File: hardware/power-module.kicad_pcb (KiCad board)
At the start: 2 copper layers, 25 x 88 mm, 37 parts, among them CN1 WJ2EDGRC-5.08-2P, K1 SRA-9VDC-CL, K2 SRA-9VDC-CL, K5 SRA-9VDC-CL, K6 SRA-9VDC-CL, Q1 SS8050_C2150, Q2 SS8050_C2150, U1 MIC5205-3.3YM5-MS, U2 PM254-2-05-W-8.5, U3 CC6903SO-10A, U4 ESP32-C3-MINI-1, U5 XC6206P332MR_C5148692, U6 L7809CV_C347291

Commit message: Add PoE board
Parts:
- removed C3: 1uF, Capacitor_SMD:C_0603_1608Metric
- removed C4: 330nF, Capacitor_SMD:C_0603_1608Metric
- removed C5: 100nF, Capacitor_SMD:C_0603_1608Metric
- removed CN1: WJ2EDGRC-5.08-2P, LCSC:CONN-TH_2P-P5.08_WJ2EDGRC-5.08-2P
- removed H1: 2*5P header, LCSC:HDR-TH_10P-P2.54-H-M-R2-C5-S2.54-W12.9
- removed K5, K6: SRA-9VDC-CL, LCSC:RELAY-TH_SRA-9VDC-CL
- removed LED4: XL-1608UYC-06, LCSC:LED0603-RD-YELLOW
- removed R4, R5, R6: 10k, Resistor_SMD:R_0603_1608Metric
- removed R9: 120, Resistor_SMD:R_0603_1608Metric
- removed REF**: WEEE-Logo_4.2x6mm_SilkScreen, Symbol:WEEE-Logo_4.2x6mm_SilkScreen
- removed U2: PM254-2-05-W-8.5, LCSC:HDR-TH_10P-P2.54-H-F-R2-C5-W8.5
- added D4: ABS10_C65028, easyeda2kicad:ABS_L5.1-W4.4-P3.35-LS6.4-TL, F.Cu at (77.2, 37.3)
- added D5: ABS10_C65028, easyeda2kicad:ABS_L5.1-W4.4-P3.35-LS6.4-TL, F.Cu at (77.2, 44.3)
- added K3: SRA-12VDC-CL, easyeda2kicad:RELAY-TH_SRA-X-CX, F.Cu at (19.0, 30.0)
- added K4: SRA-12VDC-CL, easyeda2kicad:RELAY-TH_SRA-X-CX, F.Cu at (19.0, 43.0)
- added P1: WJ2EDGRC-5.08-4P, easyeda2kicad:CONN-TH_4P-P5.08_WJ2EDGRC-5.08-4P, F.Cu at (7.40, 36.0)
- added RJ2: S22-ZZ-0019, easyeda2kicad:RJ45-TH_RT7-ZZ-0117, F.Cu at (76.0, 21.0)
- added U7: DP9900LP-12V, easyeda2kicad:PWRM-TH_DP9900LP-5V, F.Cu at (60.0, 40.0)
- K1, K2: value SRA-9VDC-CL -> SRA-12VDC-CL; footprint LCSC:RELAY-TH_SRA-9VDC-CL -> easyeda2kicad:RELAY-TH_SRA-X-CX
- U4: value ESP32-C3-MINI-1 -> ESP32-U4WDH DUAL-CORE_C20622217; footprint PCM_Espressif:ESP32-C3-MINI-1 -> easyeda2kicad:QFN-48_L5.0-W5.0-P0.35-TL-EP3.7_ESP32-U4WDH
- U6: value L7809CV_C347291 -> LAN8720A-CP-TR; footprint LCSC:TO-220-3_L10.0-W4.5-P2.54-L -> easyeda2kicad:QFN-24_L4.0-W4.0-P0.50-BL-EP2.6
- moved LED5 148.5 mm to (181.9, 26.4), turned to 0 degrees
- moved LED2 147.8 mm to (181.9, 23.7), turned to 0 degrees
- moved LED1 145.4 mm to (181.9, 21.1), turned to 0 degrees
- moved U1 138.5 mm to (183.2, 15.7), turned to 0 degrees
- moved R10 134.3 mm to (171.2, 33.5), turned to 0 degrees
- moved R7 133.6 mm to (171.2, 31.0), turned to 0 degrees
- moved R3 131.1 mm to (171.2, 28.5), turned to 0 degrees
- moved U3 130.1 mm to (15.0, 17.0), turned to 0 degrees
- moved D1 129.9 mm to (180.5, 32.4), turned to 0 degrees
- moved D3 129.2 mm to (179.6, 40.7)
- moved Q1 128.6 mm to (175.3, 30.1), turned to 0 degrees
- moved D2 126.6 mm to (179.6, 38.1)
- moved C1 126.3 mm to (171.2, 21.0)
- moved C2 123.8 mm to (171.2, 23.5)
- moved Q2 123.1 mm to (175.3, 34.4), turned to 0 degrees
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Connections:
- C1 pad 1: /TRACK POWER IN -> +12V
- C2 pad 1: /CONTROLLER POWER IN -> +3.3V
- K1 pad 1: /TRACK POWER A -> /TRACK POWER ENABLED A
- K1 pad 2: Net-(D2-A) -> unconnected-(K1-Pad2)
- K1 pad 3: /TRACK POWER ENABLED A -> Net-(D2-A)
- K1 pad 4: unconnected-(K1-Pad4) -> /RELAY POWER
- K1 pad 5: /RELAY POWER -> /TRACK POWER A
- K2 pad 1: /TRACK POWER B -> /TRACK POWER ENABLED B
- K2 pad 2: /RELAY POWER -> unconnected-(K2-Pad2)
- K2 pad 3: /TRACK POWER ENABLED B -> /RELAY POWER
- K2 pad 4: unconnected-(K2-Pad4) -> Net-(D2-A)
- K2 pad 5: Net-(D2-A) -> /TRACK POWER B
- R3 pad 1: /CONTROLLER POWER IN -> +3.3V
- U1 pad 1: /TRACK POWER IN -> +12V
- U1 pad 3: /TRACK POWER IN -> +12V
- U1 pad 5: /CONTROLLER POWER IN -> +3.3V
- U4 pad 1: GND -> unconnected-(U4-VDDA-Pad1)
- U4 pad 11: GND -> unconnected-(U4-VDET_2-Pad11)
- U4 pad 14: GND -> unconnected-(U4-GPIO25-Pad14)
- U4 pad 16: Net-(U4-GPIO10) -> unconnected-(U4-GPIO27-Pad16)
- U4 pad 18: /CURRENT SENSING INPUT -> unconnected-(U4-MTDI-Pad18)
- U4 pad 2: GND -> unconnected-(U4-LNA_IN-Pad2)
- U4 pad 20: /TRACK POWER ENABLE -> unconnected-(U4-MTCK-Pad20)
- U4 pad 21: /TRACK DIRECTION -> unconnected-(U4-MTDO-Pad21)
- U4 pad 22: Net-(U4-GPIO8) -> unconnected-(U4-GPIO2-Pad22)
- U4 pad 23: /BOOT -> unconnected-(U4-GPIO0-Pad23)
- U4 pad 26: /USB - -> unconnected-(U4-VDD_SDIO-Pad26)
- U4 pad 27: /USB + -> unconnected-(U4-GPIO17-Pad27)
- U4 pad 3: /CONTROLLER POWER IN -> unconnected-(U4-VDD3P3-Pad3)
- U4 pad 36: GND -> unconnected-(U4-GPIO23-Pad36)
- U4 pad 37: GND -> unconnected-(U4-VDD3P3_CPU-Pad37)
- U4 pad 38: GND -> unconnected-(U4-GPIO19-Pad38)
- U4 pad 39: GND -> unconnected-(U4-GPIO22-Pad39)
- U4 pad 40: GND -> unconnected-(U4-U0RXD-Pad40)
- U4 pad 41: GND -> unconnected-(U4-U0TXD-Pad41)
- U4 pad 42: GND -> unconnected-(U4-GPIO21-Pad42)
- U4 pad 43: GND -> unconnected-(U4-VDDA-Pad43)
- U4 pad 44: GND -> unconnected-(U4-XTAL_N-Pad44)
- U4 pad 45: GND -> unconnected-(U4-XTAL_P-Pad45)
- U4 pad 46: GND -> unconnected-(U4-VDDA-Pad46)
- U4 pad 47: GND -> unconnected-(U4-CAP2-Pad47)
- U4 pad 48: GND -> unconnected-(U4-CAP1-Pad48)
- U4 pad 49: GND -> unconnected-(U4-GND-Pad49)
- U4 pad 5: Net-(U4-GPIO2/ADC1_CH2) -> unconnected-(U4-SENSOR_VP-Pad5)
- U4 pad 8: /RESET -> unconnected-(U4-SENSOR_VN-Pad8)
- U6 pad 1: /TRACK POWER IN -> unconnected-(U6-VDD2A-Pad1)
- U6 pad 2: GND -> unconnected-(U6-LED2/nINTSEL-Pad2)
- U6 pad 3: /RELAY POWER -> unconnected-(U6-LED1/REGOFF-Pad3)
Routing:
- net /CONTROLLER POWER IN: track 140.3 -> 0.00 mm, vias 5 -> 0
- net GND: track 101.8 -> 0.00 mm, vias 24 -> 0
- net /TRACK POWER B: track 90.2 -> 0.00 mm
- net /CURRENT SENSING INPUT: track 85.1 -> 0.00 mm, vias 4 -> 0
- net /TRACK POWER A: track 82.8 -> 0.00 mm
- net /RELAY POWER: track 78.4 -> 0.00 mm
- net Net-(D3-A): track 66.5 -> 0.00 mm, vias 4 -> 0
- net /TRACK POWER IN: track 51.2 -> 0.00 mm, vias 2 -> 0
- net /TRACK DIRECTION: track 44.7 -> 0.00 mm, vias 2 -> 0
- net /TRACK POWER ENABLE: track 44.7 -> 0.00 mm, vias 3 -> 0
- net /TRACK POWER ENABLED B: track 43.1 -> 0.00 mm
- net Net-(U4-GPIO10): track 30.7 -> 0.00 mm, vias 2 -> 0
- net Net-(D2-A): track 30.4 -> 0.00 mm, vias 2 -> 0
- net /RESET: track 30.2 -> 0.00 mm, vias 2 -> 0
- net /TRACK POWER ENABLED A: track 28.5 -> 0.00 mm
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- removed copper zone on B.Cu, net GND
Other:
- board size 25 x 88 mm -> 85 x 50 mm
- board text removed: "12V - 24V DC 8A"
- board text removed: "8A = 70°C"
- board text removed: "ACT"
- board text removed: "DIR"
- board text removed: "ENA"
- board text removed: "PRG"
- board text removed: "PWR"
- board text removed: "networked power module"
- board text removed: "v2b"

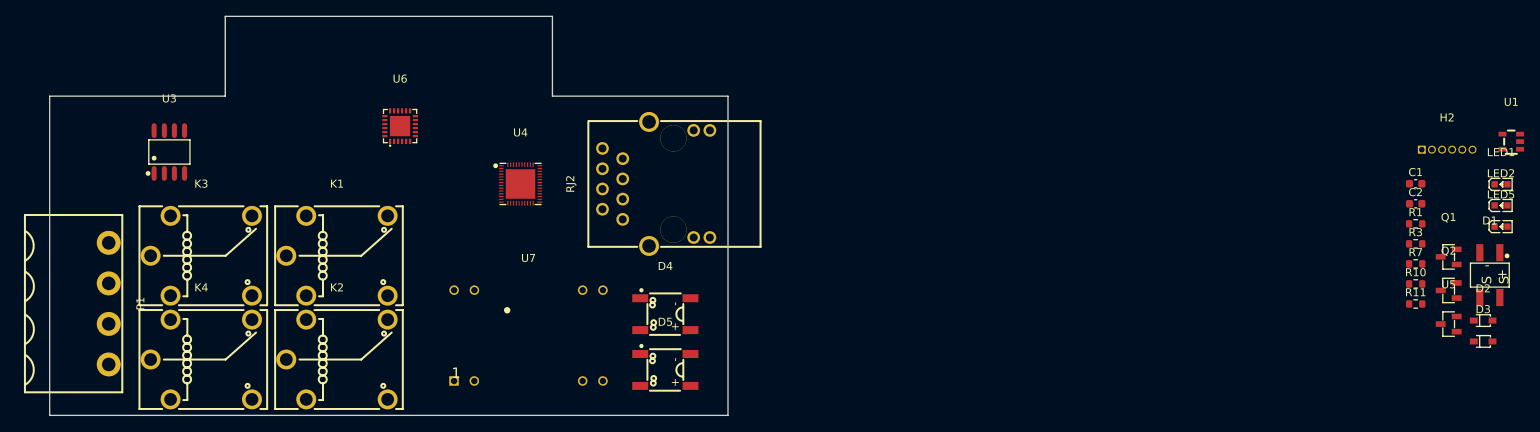
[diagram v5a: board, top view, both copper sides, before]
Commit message: Add routes and part placement
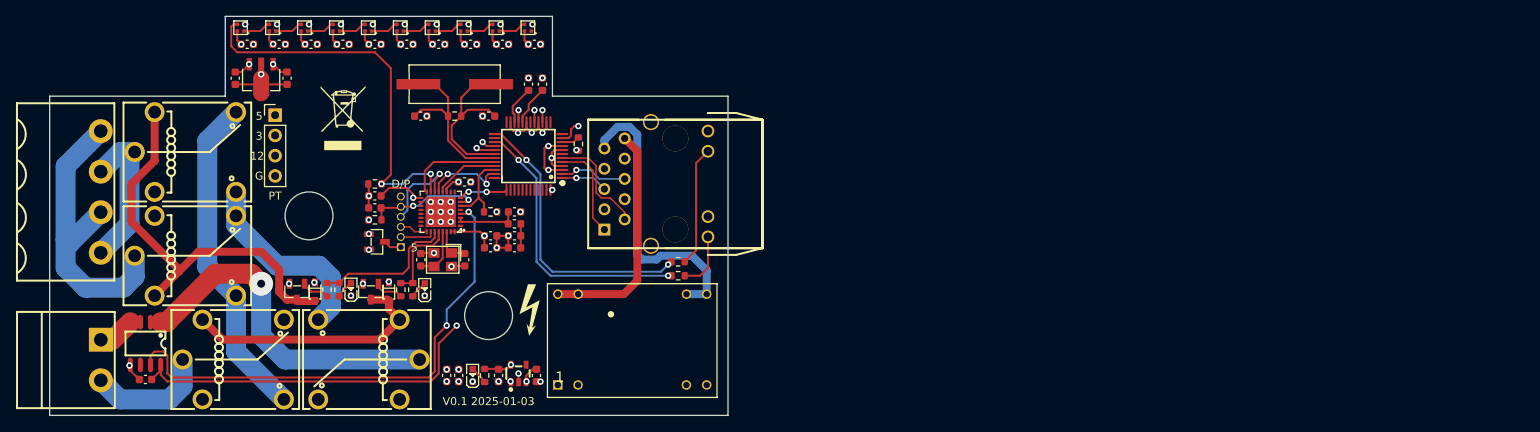
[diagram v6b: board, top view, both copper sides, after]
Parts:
- removed D3: BAS321,115, LCSC:SOD-323_L1.8-W1.3-LS2.5-RD
- removed D4, D5: ABS10_C65028, easyeda2kicad:ABS_L5.1-W4.4-P3.35-LS6.4-TL
- removed H2: DZ127R-11-06-25, LCSC:HDR-TH_6P-P1.27-V-M-A
- removed LED5: XL-1608UYC-06, LCSC:LED0603-RD-YELLOW
- removed RJ2: S22-ZZ-0019, easyeda2kicad:RJ45-TH_RT7-ZZ-0117
- added C10: 0.1uF, Capacitor_SMD:C_0603_1608Metric, F.Cu at (24.8, 3.50)
- added C11: 0.1uF, Capacitor_SMD:C_0603_1608Metric, F.Cu at (28.8, 3.50)
- added C12: 0.1uF, Capacitor_SMD:C_0603_1608Metric, F.Cu at (32.8, 3.50)
- added C13: 0.1uF, Capacitor_SMD:C_0603_1608Metric, F.Cu at (36.8, 3.50)
- added C14: 0.1uF, Capacitor_SMD:C_0603_1608Metric, F.Cu at (40.8, 3.50)
- added C15: 0.1uF, Capacitor_SMD:C_0603_1608Metric, F.Cu at (44.8, 3.50)
- added C16: 1uF, Capacitor_SMD:C_0603_1608Metric, F.Cu at (52.0, 30.5)
- added C17: 1uF, Capacitor_SMD:C_0603_1608Metric, F.Cu at (46.5, 30.5)
- added C18: 0.33uF, Capacitor_SMD:C_0603_1608Metric, F.Cu at (23.2, 7.75)
- added C19: 0.1uF, Capacitor_SMD:C_0603_1608Metric, F.Cu at (29.8, 7.75)
- added C20: 0.1nF, Capacitor_SMD:C_0603_1608Metric, F.Cu at (12.0, 45.5)
- added C21: 1uF, Capacitor_SMD:C_0603_1608Metric, F.Cu at (55.2, 29.0)
- added C22: 10nF, Capacitor_SMD:C_0603_1608Metric, F.Cu at (55.2, 27.5)
- added C23: 0.1uF, Capacitor_SMD:C_0603_1608Metric, F.Cu at (52.0, 20.8)
- added C24: 0.1uF, Capacitor_SMD:C_0603_1608Metric, F.Cu at (40.8, 22.5)
- added C25: 1uF, Capacitor_SMD:C_0603_1608Metric, F.Cu at (58.2, 24.5)
- added C26: 0.1uF, Capacitor_SMD:C_0603_1608Metric, F.Cu at (58.2, 27.5)
- added C27: 10uF, Capacitor_SMD:C_0603_1608Metric, F.Cu at (58.2, 29.0)
- added C28: 0.1uF, Capacitor_SMD:C_0603_1608Metric, F.Cu at (48.8, 3.50)
- added C29: 0.1uF, Capacitor_SMD:C_0603_1608Metric, F.Cu at (52.8, 3.50)
- added C3: 100uF 25V, Capacitor_SMD:C_0603_1608Metric, F.Cu at (49.8, 45.0)
- added C30: 0.1uF, Capacitor_SMD:C_0603_1608Metric, F.Cu at (56.8, 3.50)
- added C31: 0.1uF, Capacitor_SMD:C_0603_1608Metric, F.Cu at (60.8, 3.50)
- added C4: 10uF 25V, Capacitor_SMD:C_0603_1608Metric, F.Cu at (51.2, 45.0)
- added C5: 4.7uF, Capacitor_SMD:C_0603_1608Metric, F.Cu at (61.8, 8.50)
- added C6: 4.7uF, Capacitor_SMD:C_0603_1608Metric, F.Cu at (60.0, 8.50)
- added C7: 4.7uF, Capacitor_SMD:C_0603_1608Metric, F.Cu at (55.0, 12.5)
- added C8: 4.7uF, Capacitor_SMD:C_0603_1608Metric, F.Cu at (46.5, 12.5)
- added C9: 1uF, Capacitor_SMD:C_0603_1608Metric, F.Cu at (40.8, 24.0)
- added CN1: WJ2EDGRC-5.08-2P, easyeda2kicad:CONN-TH_2P-P5.08_WJ2EDGRC-5.08-2P, F.Cu at (6.41, 43.1)
- added H1: DZ127R-11-06-25, easyeda2kicad:HDR-TH_6P-P1.27-V-M-A, F.Cu at (44.0, 25.8)
- added J1: Conn_01x04_Pin, Connector_PinHeader_2.54mm:PinHeader_1x04_P2.54mm_Vertical, F.Cu at (28.2, 12.4)
- added L1: 2.0nH, Inductor_SMD:L_0603_1608Metric, F.Cu at (58.2, 26.0)
- added LED3: XL-1608UYC-06, easyeda2kicad:LED0603-RD-YELLOW, F.Cu at (37.8, 34.2)
- added R12: 10K, Resistor_SMD:R_0603_1608Metric, F.Cu at (40.8, 21.0)
- added R2: 56, Resistor_SMD:R_0603_1608Metric, F.Cu at (78.8, 32.5)
- added R4: 56, Resistor_SMD:R_0603_1608Metric, F.Cu at (78.8, 30.8)
- added R5: 12.4K 1%, Resistor_SMD:R_0603_1608Metric, F.Cu at (66.2, 16.0)
- added R6: 1M, Resistor_SMD:R_0603_1608Metric, F.Cu at (50.8, 12.5)
- added R8: 10K, Resistor_SMD:R_0603_1608Metric, F.Cu at (55.2, 24.5)
- added R9: 10K, Resistor_SMD:R_0603_1608Metric, F.Cu at (40.8, 25.5)
- added REF**: WEEE-Logo_5.6x8mm_SilkScreen, Symbol:WEEE-Logo_5.6x8mm_SilkScreen, F.Cu at (36.8, 12.8)
- added RJ1: HY931147C, easyeda2kicad:RJ45-TH_HY931147C, F.Cu at (76.0, 21.0)
- added U10: XL-1010RGBC-WS2812B, easyeda2kicad:LED-SMD_4P-L1.0-W1.0-TL_XL-1010RGBC-WS2812B, F.Cu at (35.9, 1.42)
- added U11: XL-1010RGBC-WS2812B, easyeda2kicad:LED-SMD_4P-L1.0-W1.0-TL_XL-1010RGBC-WS2812B, F.Cu at (39.9, 1.42)
- added U12: XL-1010RGBC-WS2812B, easyeda2kicad:LED-SMD_4P-L1.0-W1.0-TL_XL-1010RGBC-WS2812B, F.Cu at (43.9, 1.42)
- added U13: L327S400H11L, easyeda2kicad:CRYSTAL-SMD_4P-L3.2-W2.5-BL, F.Cu at (49.2, 30.5)
- added U14: UMW78L05, easyeda2kicad:SOT-89-3_L4.5-W2.5-P1.50-LS4.2-BR, F.Cu at (26.5, 7.36)
- added U15: XL-1010RGBC-WS2812B, easyeda2kicad:LED-SMD_4P-L1.0-W1.0-TL_XL-1010RGBC-WS2812B, F.Cu at (47.9, 1.42)
- added U16: XL-1010RGBC-WS2812B, easyeda2kicad:LED-SMD_4P-L1.0-W1.0-TL_XL-1010RGBC-WS2812B, F.Cu at (51.9, 1.42)
- added U17: XL-1010RGBC-WS2812B, easyeda2kicad:LED-SMD_4P-L1.0-W1.0-TL_XL-1010RGBC-WS2812B, F.Cu at (55.9, 1.42)
- added U18: XL-1010RGBC-WS2812B, easyeda2kicad:LED-SMD_4P-L1.0-W1.0-TL_XL-1010RGBC-WS2812B, F.Cu at (59.9, 1.42)
- added U2: CC6903SO-10A, easyeda2kicad:SOP-8_L4.9-W3.9-P1.27-LS6.0-BL, F.Cu at (12.0, 41.0)
- added U8: XL-1010RGBC-WS2812B, easyeda2kicad:LED-SMD_4P-L1.0-W1.0-TL_XL-1010RGBC-WS2812B, F.Cu at (27.9, 1.42)
- added U9: XL-1010RGBC-WS2812B, easyeda2kicad:LED-SMD_4P-L1.0-W1.0-TL_XL-1010RGBC-WS2812B, F.Cu at (31.9, 1.42)
- added X1: X49SM25MSD2SC, easyeda2kicad:HC-49S_L11.4-W4.8, F.Cu at (50.8, 8.50)
- D1: value MB10FH5G0NP -> BAS321,115; footprint LCSC:MBF_L4.8-W3.9-P2.50-LS6.7-TR -> easyeda2kicad:SOD-323_L1.8-W1.3-LS2.5-RD
- D2: footprint LCSC:SOD-323_L1.8-W1.3-LS2.5-RD -> easyeda2kicad:SOD-323_L1.8-W1.3-LS2.5-RD
- LED1, LED2: footprint LCSC:LED0603-RD-YELLOW -> easyeda2kicad:LED0603-RD-YELLOW
- Q1, Q2, U5: footprint LCSC:SOT-23-3_L2.9-W1.3-P1.90-LS2.4-BR -> easyeda2kicad:SOT-23-3_L2.9-W1.3-P1.90-LS2.4-BR
- U1: footprint LCSC:SOT-23-5_L2.9-W1.6-P0.95-LS2.8-BR -> easyeda2kicad:SOT-23-5_L2.9-W1.6-P0.95-LS2.8-BR
- U3: value CC6903SO-10A -> W5500; footprint LCSC:SOP-8_L4.9-W3.9-P1.27-LS6.0-BL -> easyeda2kicad:LQFP-48_L7.0-W7.0-P0.50-LS9.0-BL
- U4: value ESP32-U4WDH DUAL-CORE_C20622217 -> ESP32-C3FH4; footprint easyeda2kicad:QFN-48_L5.0-W5.0-P0.35-TL-EP3.7_ESP32-U4WDH -> easyeda2kicad:QFN-32_L5.0-W5.0-P0.50-TL-EP3.7
- U6: value LAN8720A-CP-TR -> XL-1010RGBC-WS2812B; footprint easyeda2kicad:QFN-24_L4.0-W4.0-P0.50-BL-EP2.6 -> easyeda2kicad:LED-SMD_4P-L1.0-W1.0-TL_XL-1010RGBC-WS2812B
- moved D2 146.4 mm to (33.2, 34.5), turned to -90 degrees
- moved Q1 144.4 mm to (31.0, 34.5), turned to 90 degrees
- moved D1 138.0 mm to (42.5, 34.5), turned to -90 degrees
- moved R11 136.4 mm to (34.8, 34.2), turned to 90 degrees
- moved LED2 135.3 mm to (47.0, 34.2), turned to 90 degrees
- moved Q2 135.1 mm to (40.2, 34.5), turned to 90 degrees
- moved R10 134.9 mm to (36.2, 34.2), turned to 90 degrees
- moved U5 134.7 mm to (41.0, 28.2), turned to 180 degrees
- moved LED1 131.1 mm to (53.0, 45.0), turned to 90 degrees
- moved U1 127.7 mm to (58.8, 44.8), turned to -90 degrees
- moved R1 127.4 mm to (44.0, 34.2), turned to 90 degrees
- moved R7 125.7 mm to (45.5, 34.2), turned to 90 degrees
- moved R3 117.8 mm to (54.5, 45.0), turned to -90 degrees
- moved C2 116.9 mm to (56.2, 45.0), turned to -90 degrees
- moved C1 112.8 mm to (61.0, 45.0), turned to -90 degrees
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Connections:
- D1 pad 1: /TRACK POWER IN -> +12V
- D1 pad 2: /TRACK POWER A -> Net-(D1-A)
- D2 pad 1: /RELAY POWER -> +12V
- K1 pad 3: Net-(D2-A) -> Net-(D1-A)
- K1 pad 4: /RELAY POWER -> +12V
- K2 pad 3: /RELAY POWER -> +12V
- K2 pad 4: Net-(D2-A) -> Net-(D1-A)
- K3 pad 3: Net-(D3-A) -> Net-(D2-A)
- K3 pad 4: /RELAY POWER -> +12V
- K4 pad 3: /RELAY POWER -> +12V
- K4 pad 4: Net-(D3-A) -> Net-(D2-A)
- P1 pad 2: Net-(P1-Pad2) -> /TRACK OUT A
- P1 pad 4: Net-(P1-Pad2) -> /TRACK OUT A
- Q1 pad 3: Net-(D3-A) -> Net-(D2-A)
- Q2 pad 3: Net-(D2-A) -> Net-(D1-A)
- U3 pad 1: /TRACK OUT A -> /ETHERNET TX -
- U3 pad 2: /TRACK OUT A -> /ETHERNET TX +
- U3 pad 3: Net-(P1-Pad2) -> GND
- U3 pad 4: Net-(P1-Pad2) -> +3.3V
- U3 pad 5: GND -> /ETHERNET RX -
- U3 pad 6: unconnected-(U3-NC-Pad6) -> /ETHERNET RX +
- U3 pad 7: /CURRENT SENSING INPUT -> unconnected-(U3-DNC-Pad7)
- U3 pad 8: /CONTROLLER POWER IN -> +3.3V
- U4 pad 11: unconnected-(U4-VDET_2-Pad11) -> +3.3V
- U4 pad 12: unconnected-(U4-32K_XP-Pad12) -> /WIZ SPI SCLK
- U4 pad 13: unconnected-(U4-32K_XN-Pad13) -> /WIZ SPI MOSI
- U4 pad 14: unconnected-(U4-GPIO25-Pad14) -> /BOOT
- U4 pad 15: unconnected-(U4-GPIO26-Pad15) -> /LED DATA IN
- U4 pad 16: unconnected-(U4-GPIO27-Pad16) -> /WIZ SPI CS
- U4 pad 17: unconnected-(U4-MTMS-Pad17) -> +3.3V
- U4 pad 2: unconnected-(U4-LNA_IN-Pad2) -> Net-(C25-Pad2)
- U4 pad 25: unconnected-(U4-GPIO16-Pad25) -> /USB -
- U4 pad 26: unconnected-(U4-VDD_SDIO-Pad26) -> /USB +
- U4 pad 27: unconnected-(U4-GPIO17-Pad27) -> /TRACK DIRECTION
- U4 pad 28: unconnected-(U4-SD_DATA_2-Pad28) -> /TRACK POWER ENABLE
- U4 pad 29: unconnected-(U4-SD_DATA_3-Pad29) -> Net-(U4-XTAL_N)
- U4 pad 3: unconnected-(U4-VDD3P3-Pad3) -> Net-(C25-Pad2)
- U4 pad 30: unconnected-(U4-SD_CMD-Pad30) -> Net-(U4-XTAL_P)
- U4 pad 31: unconnected-(U4-SD_CLK-Pad31) -> +3.3V
- U4 pad 32: unconnected-(U4-SD_DATA_0-Pad32) -> +3.3V
- U4 pad 33: unconnected-(U4-SD_DATA_1-Pad33) -> GND
- U4 pad 4: unconnected-(U4-VDD3P3-Pad4) -> /CURRENT SENSING INPUT
- U4 pad 6: unconnected-(U4-SENSOR_CAPP-Pad6) -> /WIZ SPI MISO
- U4 pad 7: unconnected-(U4-SENSOR_CAPN-Pad7) -> /RESET
- U4 pad 8: unconnected-(U4-SENSOR_VN-Pad8) -> /WIZ RESET
- U5 pad 2: /CONTROLLER POWER IN -> +3.3V
- U6 pad 1: unconnected-(U6-VDD2A-Pad1) -> Net-(U6-DOUT)
- U6 pad 2: unconnected-(U6-LED2/nINTSEL-Pad2) -> +5V
- U6 pad 3: unconnected-(U6-LED1/REGOFF-Pad3) -> GND
- U6 pad 4: unconnected-(U6-XTAL2-Pad4) -> /LED DATA IN
- U7 pad 1: unconnected-(U7-+VDC-Pad1) -> +12V
- U7 pad 2: unconnected-(U7-+VDC-Pad2) -> +12V
- U7 pad 3: unconnected-(U7--VDC-Pad3) -> GND
- U7 pad 5: unconnected-(U7-VIN+-Pad5) -> /POE IN +
- U7 pad 6: unconnected-(U7-VIN+-Pad6) -> /POE IN +
- U7 pad 7: unconnected-(U7-VIN--Pad7) -> /POE IN -
- U7 pad 8: unconnected-(U7-VIN--Pad8) -> /POE IN -
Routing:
- net +3.3V: track 0.00 -> 77.8 mm, vias 0 -> 14
- net /CURRENT SENSING INPUT: track 0.00 -> 63.5 mm, vias 0 -> 2
- net GND: track 0.00 -> 56.4 mm, vias 0 -> 61
- net Net-(D2-A): track 0.00 -> 50.2 mm
- net /LED DATA IN: track 0.00 -> 48.4 mm, vias 0 -> 2
- net /TRACK POWER B: track 0.00 -> 43.2 mm, vias 0 -> 1
- net /TRACK POWER ENABLED A: track 0.00 -> 41.5 mm
- net /POE IN +: track 0.00 -> 38.1 mm
- net /TRACK OUT B: track 0.00 -> 38.0 mm
- net /LED LINK: track 0.00 -> 36.1 mm, vias 0 -> 2
- net /LED ACTIVITY: track 0.00 -> 35.3 mm, vias 0 -> 2
- net Net-(D1-A): track 0.00 -> 32.3 mm
- net /POE IN -: track 0.00 -> 29.1 mm
- net /TRACK POWER ENABLED B: track 0.00 -> 24.7 mm
- net Net-(U3-XI/CLKIN): track 0.00 -> 21.8 mm
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- added copper zone on In1.Cu, net +12V
- added copper zone on In1.Cu, net +3.3V
- added copper zone on In1.Cu, net +5V
- added copper zone on In2.Cu, net GND
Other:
- outline, holes or cut-outs redrawn
- copper layers 2 -> 4
- board text added: "12"
- board text added: "15°C"
- board text added: "20°C"
- board text added: "25°C"
- board text added: "3"
- board text added: "30°C"
- board text added: "4.5A"
- board text added: "5"
- board text added: "5.2A"
- board text added: "5.7A"
- board text added: "50V"
- board text added: "6.2A"
- board text added: "6A 50V"
- board text added: "Components: 10A Traces: 6A at 2oz"
- board text added: "Current"
- board text added: "D/P"
- board text added: "G"
- board text added: "Metered"
- board text added: "PDM-6M-ERM-NEP"
- board text added: "PT"
- board text added: "PoE 802.3af"
- board text added: "T rise"
- board text added: "V0.1 2025-01-03"
- board text added: "power district module"

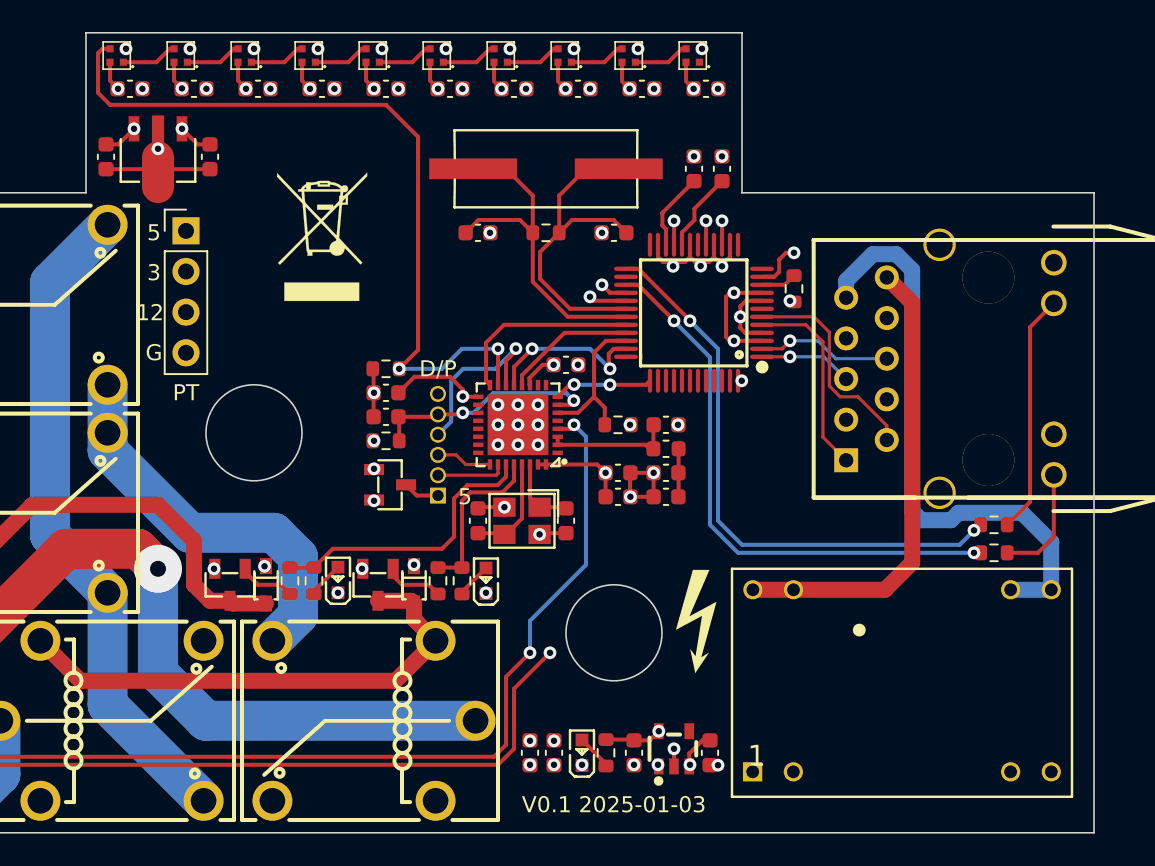
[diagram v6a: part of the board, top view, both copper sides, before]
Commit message: Fix SPI pins, power supply current
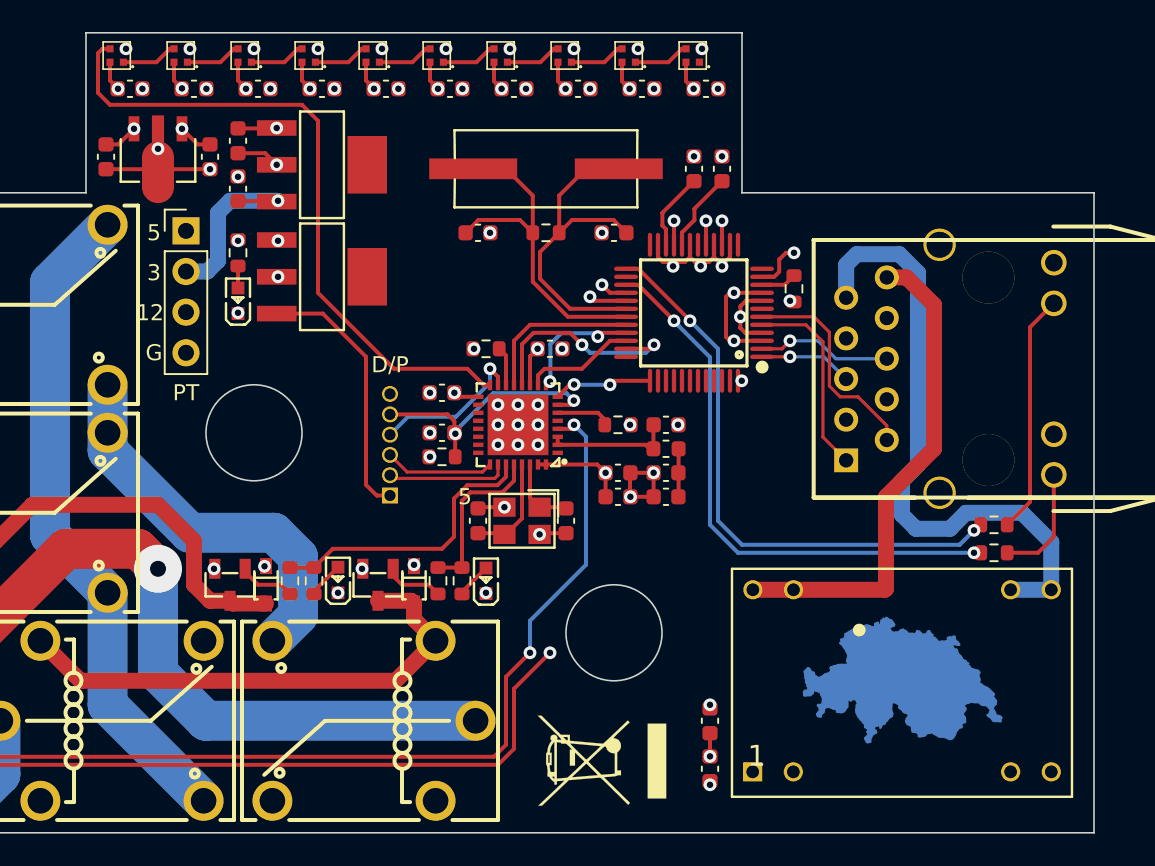
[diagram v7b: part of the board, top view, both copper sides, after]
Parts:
- C1: value 1uF -> 0.1nF
- C2: value 2.2uF -> 0.1nF
- U1: value MIC5205-3.3YM5-MS -> AMS1117-3.3_C347222; footprint easyeda2kicad:SOT-23-5_L2.9-W1.6-P0.95-LS2.8-BR -> easyeda2kicad:SOT-223-4_L6.5-W3.5-P2.30-LS7.0-BR
- U5: value XC6206P332MR_C5148692 -> AMS1117-3.3_C347222; footprint easyeda2kicad:SOT-23-3_L2.9-W1.3-P1.90-LS2.4-BR -> easyeda2kicad:SOT-223-4_L6.5-W3.5-P2.30-LS7.0-BR
- moved C1 48.3 mm to (31.5, 6.75), turned to 90 degrees
- moved C2 43.1 mm to (31.5, 9.75), turned to 90 degrees
- moved U1 42.6 mm to (36.8, 8.25), turned to 180 degrees
- moved R3 38.8 mm to (31.5, 13.8)
- moved REF** 37.1 mm to (54.2, 45.5), turned to 90 degrees
- moved LED1 35.5 mm to (31.5, 16.8)
- moved U5 13.7 mm to (36.8, 15.2)
- moved C3 11.4 mm to (61.0, 43.0)
- moved C4 9.80 mm to (61.0, 46.0), turned to 90 degrees
- moved R12 6.37 mm to (47.0, 19.8)
- moved C9 3.64 mm to (44.2, 25.0)
- moved R9 3.64 mm to (44.2, 26.5)
- moved C24 3.50 mm to (44.2, 22.5)
- moved H1 3.00 mm to (41.0, 25.8)
- moved C23 1.41 mm to (51.0, 19.8)
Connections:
- C1 pad 1: +12V -> +3.3V
- C2 pad 1: +3.3V -> +12V
- R12 pad 2: /LED DATA IN -> Net-(U4-GPIO8)
- R8 pad 1: /WIZ SPI MISO -> Net-(U4-GPIO2)
- U1 pad 1: +12V -> GND
- U1 pad 2: GND -> +3.3V
- U4 pad 10: unconnected-(U4-MTDI-Pad10) -> /WIZ SPI MISO
- U4 pad 12: /WIZ SPI SCLK -> /WIZ SPI MOSI
- U4 pad 13: /WIZ SPI MOSI -> /WIZ SPI CS
- U4 pad 14: /BOOT -> Net-(U4-GPIO8)
- U4 pad 15: /LED DATA IN -> /BOOT
- U4 pad 16: /WIZ SPI CS -> /LED DATA IN
- U4 pad 6: /WIZ SPI MISO -> Net-(U4-GPIO2)
- U4 pad 9: unconnected-(U4-MTMS-Pad9) -> /WIZ SPI SCLK
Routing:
- net Net-(U5-VIN): track 2.28 -> 16.5 mm
- net +12V: track 5.32 -> 15.6 mm, vias 7 -> 5
- net /LED DATA IN: track 48.4 -> 41.7 mm, vias 2 -> 0
- net +3.3V: track 77.8 -> 72.9 mm, vias 14 -> 15
- net Net-(U4-GPIO2): track 0.00 -> 3.45 mm
- net /USB -: track 3.50 -> 6.89 mm
- net /WIZ SPI MOSI: track 10.3 -> 13.7 mm
- net /USB +: track 4.36 -> 7.59 mm
- net /WIZ SPI MISO: track 9.77 -> 7.01 mm
- net Net-(U4-GPIO8): track 0.00 -> 2.45 mm
- net /RESET: track 14.4 -> 16.3 mm
- net /POE IN -: track 29.1 -> 31.0 mm
- net /WIZ SPI CS: track 12.0 -> 10.2 mm
- net /BOOT: track 11.1 -> 9.70 mm
- net GND: track 56.4 -> 55.1 mm, vias 61 -> 63
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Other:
- board text added: "V0.1"
- board text removed: "50V"
- board text removed: "V0.1 2025-01-03"
